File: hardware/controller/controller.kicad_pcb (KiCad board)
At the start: 4 copper layers, 57 x 47 mm, 50 parts, among them J1 Conn_01x02_Pin, J11 Barrel_Jack, J12 USB_C_Receptacle_USB2.0_14P, J2 Conn_01x02_Pin, J3 Conn_01x02_Pin, J5 Screw_Terminal_01x02, J6 Screw_Terminal_01x02, J7 Conn_01x04_Pin, J8 Conn_01x04_Pin, U1 ESP32-C3-MINI-1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

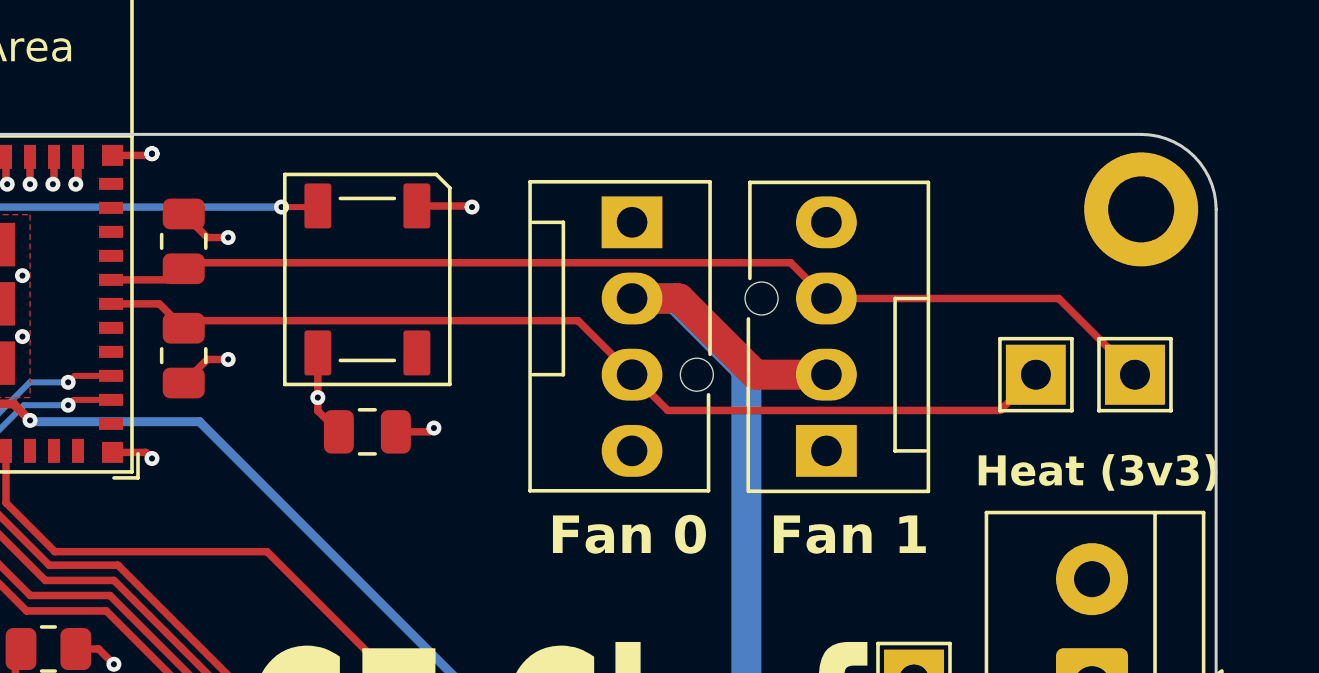
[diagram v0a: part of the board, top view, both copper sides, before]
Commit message: Fix resistor on regulator, space out fan headers more
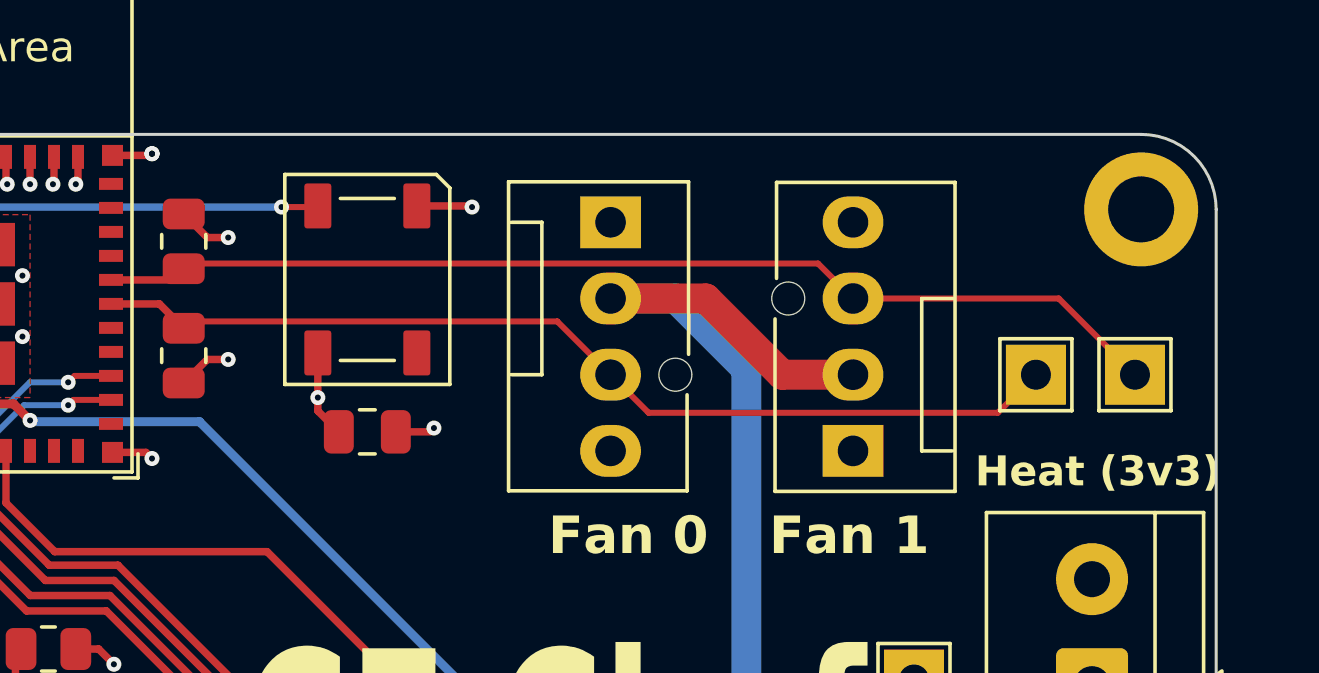
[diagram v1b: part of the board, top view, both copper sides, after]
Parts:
- R9: value 75k -> 24k
- moved J8 0.89 mm to (152.1, 82.5)
- moved J7 0.72 mm to (144.1, 74.9)
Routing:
- net +12V: track 83.3 -> 85.6 mm
